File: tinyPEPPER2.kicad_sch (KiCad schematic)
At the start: 15 parts, among them U1 AP131-30

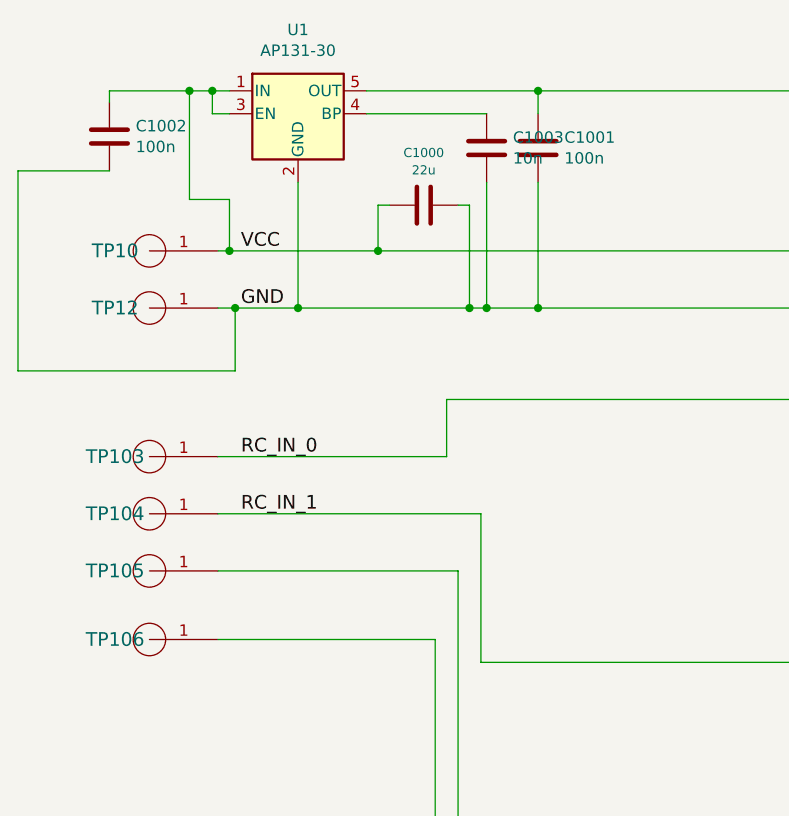
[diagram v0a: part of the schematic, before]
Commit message: cleaning up schematic
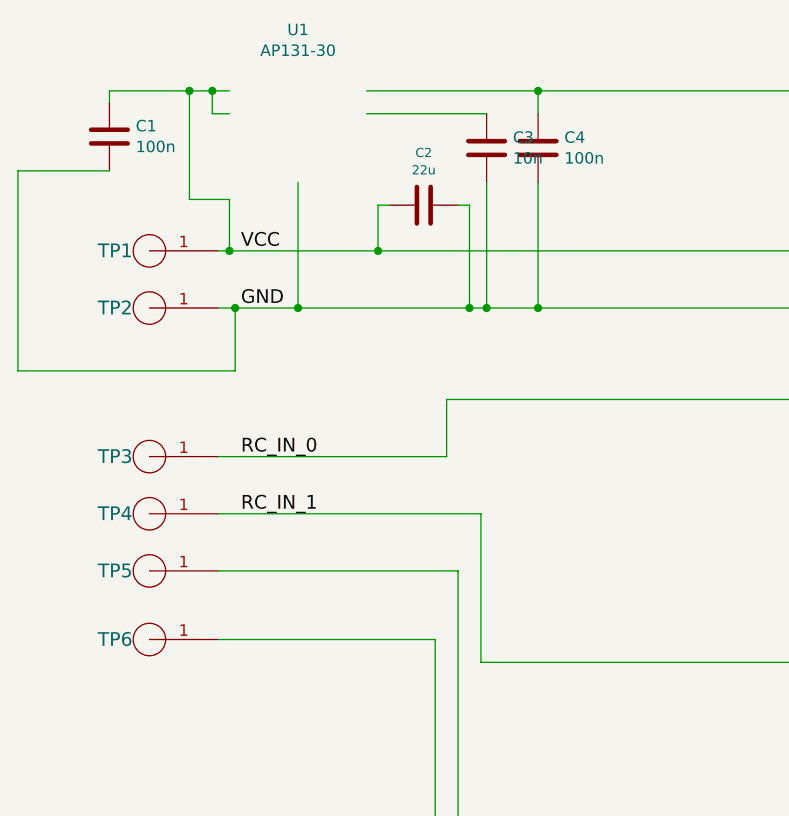
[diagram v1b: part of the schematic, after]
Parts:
- renumbered C1002 to C1, C1000 to C2, C1003 to C3, C1001 to C4, TP10 to TP1, TP12 to TP2, TP103 to TP3, TP104 to TP4, TP105 to TP5, TP106 to TP6
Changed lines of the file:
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@@
 		(in_pos_files yes)
 		(dnp no)
-		(property "Reference" "TP10"
+		(property "Reference" "TP1"
 			(at 36.83 62.23 0)
 			(show_name no)
@@
 			(project "tinyPEPPER2"
 				(path "/b5480a8a-eaf5-4e3b-b19a-0cc821568b0c"
-					(reference "TP10")
+					(reference "TP1")
 					(unit 1)
 				)
@@
 		(in_pos_files yes)
 		(dnp no)
-		(property "Reference" "TP12"
+		(property "Reference" "TP2"
 			(at 36.83 68.58 0)
 			(show_name no)
@@
 			(project "tinyPEPPER2"
 				(path "/b5480a8a-eaf5-4e3b-b19a-0cc821568b0c"
-					(reference "TP12")
+					(reference "TP2")
 					(unit 1)
 				)
@@
 		(in_pos_files yes)
 		(dnp no)
-		(property "Reference" "TP103"
+		(property "Reference" "TP3"
 			(at 36.83 85.09 0)
 			(show_name no)
@@
 			(project "tinyPEPPER2"
 				(path "/b5480a8a-eaf5-4e3b-b19a-0cc821568b0c"
-					(reference "TP103")
+					(reference "TP3")
 					(unit 1)
 				)
@@
 		(in_pos_files yes)
 		(dnp no)
-		(property "Reference" "TP104"
+		(property "Reference" "TP4"
 			(at 36.83 91.44 0)
 			(show_name no)
@@
 			(project "tinyPEPPER2"
 				(path "/b5480a8a-eaf5-4e3b-b19a-0cc821568b0c"
-					(reference "TP104")
+					(reference "TP4")
 					(unit 1)
 				)
@@
 		(in_pos_files yes)
 		(dnp no)
-		(property "Reference" "TP105"
+		(property "Reference" "TP5"
 			(at 36.83 97.79 0)
 			(show_name no)
@@
 			(project "tinyPEPPER2"
 				(path "/b5480a8a-eaf5-4e3b-b19a-0cc821568b0c"
-					(reference "TP105")
+					(reference "TP5")
 					(unit 1)
 				)
@@
 		(in_pos_files yes)
 		(dnp no)
-		(property "Reference" "TP106"
+		(property "Reference" "TP6"
 			(at 36.83 105.41 0)
 			(show_name no)
@@
 			(project "tinyPEPPER2"
 				(path "/b5480a8a-eaf5-4e3b-b19a-0cc821568b0c"
-					(reference "TP106")
+					(reference "TP6")
 					(unit 1)
 				)
@@
 		(in_pos_files yes)
 		(dnp no)
-		(property "Reference" "C1000"
+		(property "Reference" "C2"
 			(at 71.12 51.3334 90)
 			(show_name no)
@@
 			(project "tinyPEPPER2"
 				(path "/b5480a8a-eaf5-4e3b-b19a-0cc821568b0c"
-					(reference "C1000")
+					(reference "C2")
 					(unit 1)
 				)
@@
 		(in_pos_files yes)
 		(dnp no)
-		(property "Reference" "C1001"
+		(property "Reference" "C4"
 			(at 86.741 49.6316 0)
 			(show_name no)
@@
 			)
 		)
-		(instances
-			(project "tinyPEPPER2"
-				(path "/b5480a8a-eaf5-4e3b-b19a-0cc821568b0c"
-					(reference "C1001")
+		(pin "1"
+		)
+		(pin "2"
+		)
+		(instances
+			(project "tinyPEPPER2"
+				(path "/b5480a8a-eaf5-4e3b-b19a-0cc821568b0c"
+					(reference "C4")
 					(unit 1)
 				)
@@
 		(in_pos_files yes)
 		(dnp no)
-		(property "Reference" "C1002"
+		(property "Reference" "C1"
 			(at 39.116 48.3616 0)
 			(show_name no)
@@
 			)
 		)
-		(instances
-			(project "tinyPEPPER2"
-				(path "/b5480a8a-eaf5-4e3b-b19a-0cc821568b0c"
-					(reference "C1002")
+		(pin "1"
+		)
+		(pin "2"
+		)
+		(instances
+			(project "tinyPEPPER2"
+				(path "/b5480a8a-eaf5-4e3b-b19a-0cc821568b0c"
+					(reference "C1")
 					(unit 1)
 				)
@@
 		(in_pos_files yes)
 		(dnp no)
-		(property "Reference" "C1003"
+		(property "Reference" "C3"
 			(at 81.026 49.6316 0)
 			(show_name no)
@@
 			)
 		)
-		(instances
-			(project "tinyPEPPER2"
-				(path "/b5480a8a-eaf5-4e3b-b19a-0cc821568b0c"
-					(reference "C1003")
-					(unit 1)
-				)
+		(pin "1"
+		)
+		(pin "2"
+		)
+		(instances
+			(project "tinyPEPPER2"
+				(path "/b5480a8a-eaf5-4e3b-b19a-0cc821568b0c"
+					(reference "C3")
+					(unit 1)
+				)

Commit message: fix ap131-30
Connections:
- net GND: now also U1.2 (GND)
- net VCC: now also U1.1 (IN), U1.3 (EN)
- net single esc 1/3V3: now also U1.5 (OUT)
- net at C3.1: now also U1.4 (BP)

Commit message: add pwr lines to schematic
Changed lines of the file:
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@@
 	(paper "A4")
 	(title_block
-		(date "7 oct 2016")
+		(date "2026-10-02")
 	)
 	(junction
@@
 	)
 	(junction
+		(at 48.26 68.58)
+		(diameter 0)
+		(color 0 0 0 0)
+	)
+	(junction
 		(at 47.625 44.45)
 		(diameter 0)
@@
 	)
 	(junction
+		(at 48.26 62.23)
+		(diameter 0)
+		(color 0 0 0 0)
+	)
+	(junction
 		(at 45.085 44.45)
 		(diameter 0)
@@
 	(wire
 		(pts
+			(xy 30.48 58.42) (xy 48.26 58.42)
+		)
+		(stroke
+			(width 0)
+			(type default)
+		)
+	)
+	(wire
+		(pts
 			(xy 167.64 151.765) (xy 189.865 151.765)
 		)
@@
 	(wire
 		(pts
+			(xy 48.26 73.66) (xy 48.26 68.58)
+		)
+		(stroke
+			(width 0)
+			(type default)
+		)
+	)
+	(wire
+		(pts
 			(xy 48.26 68.58) (xy 119.38 68.58)
 		)
@@
 	(wire
 		(pts
+			(xy 48.26 58.42) (xy 48.26 62.23)
+		)
+		(stroke
+			(width 0)
+			(type default)
+		)
+	)
+	(wire
+		(pts
 			(xy 83.82 54.61) (xy 83.82 68.58)
 		)
@@
 		(pts
 			(xy 189.865 151.765) (xy 189.865 44.45)
+		)
+		(stroke
+			(width 0)
+			(type default)
+		)
+	)
+	(wire
+		(pts
+			(xy 29.21 73.66) (xy 48.26 73.66)
 		)
 		(stroke
@@
 			)
 		)
+		(pin "1"
+		)
+		(pin "2"
+		)
+		(pin "3"
+		)
+		(pin "4"
+		)
+		(pin "5"
+		)
 		(instances
 			(project "tinyPEPPER2"
@@
 					(unit 1)
 				)
+			)
+		)
+	)
+	(symbol
+		(lib_id "custom:PWR_FLAG")
+		(at 30.48 58.42 0)
+		(unit 1)
+		(body_style 1)
+		(exclude_from_sim no)
+		(in_bom yes)
+		(on_board yes)
+		(in_pos_files yes)
+		(dnp no)
+		(fields_autoplaced yes)
+		(property "Reference" "#FLG01"
+			(at 30.48 56.515 0)
+			(hide yes)
+			(show_name no)
+			(do_not_autoplace no)
+			(effects
+				(font
+					(size 1.27 1.27)
+				)
+			)
+		)
+		(property "Value" "PWR_FLAG"
+			(at 30.48 53.34 0)
+			(show_name no)
+			(do_not_autoplace no)
+			(effects
+				(font
+					(size 1.27 1.27)
+				)
+			)
+		)
+		(property "Footprint" ""
+			(at 30.48 58.42 0)
+			(hide yes)
+			(show_name no)
+			(do_not_autoplace no)
+			(effects
+				(font
+					(size 1.27 1.27)
+				)
+			)
+		)
+		(property "Datasheet" ""
+			(at 30.48 58.42 0)
+			(hide yes)
+			(show_name no)
+			(do_not_autoplace no)
+			(effects
+				(font
+					(size 1.27 1.27)
+				)
+			)
+		)
+		(property "Description" "Special symbol for telling ERC where power comes from"
+			(at 30.48 58.42 0)
+			(hide yes)
+			(show_name no)
+			(do_not_autoplace no)
+			(effects
+				(font
+					(size 1.27 1.27)
+				)
+			)
+		)
+		(pin "1"
+		)
+		(instances
+			(project "tinyPEPPER2"
+				(path "/b5480a8a-eaf5-4e3b-b19a-0cc821568b0c"
+					(reference "#FLG01")
+					(unit 1)
+				)
+			)
+		)
+	)
+	(symbol
+		(lib_id "custom:PWR_FLAG")
+		(at 29.21 73.66 0)
+		(unit 1)
+		(body_style 1)
+		(exclude_from_sim no)
+		(in_bom yes)
+		(on_board yes)
+		(in_pos_files yes)
+		(dnp no)
+		(fields_autoplaced yes)
+		(property "Reference" "#FLG02"
+			(at 29.21 71.755 0)
+			(hide yes)
+			(show_name no)
+			(do_not_autoplace no)
+			(effects
+				(font
+					(size 1.27 1.27)
+				)
+			)
+		)
+		(property "Value" "PWR_FLAG"
+			(at 29.21 68.58 0)
+			(show_name no)
+			(do_not_autoplace no)
+			(effects
+				(font
+					(size 1.27 1.27)
+				)
+			)
+		)
+		(property "Footprint" ""
+			(at 29.21 73.66 0)
+			(hide yes)
+			(show_name no)
+			(do_not_autoplace no)
+			(effects
+				(font
+					(size 1.27 1.27)
+				)
+			)
+		)
+		(property "Datasheet" ""
+			(at 29.21 73.66 0)
+			(hide yes)
+			(show_name no)
+			(do_not_autoplace no)
+			(effects
+				(font
+					(size 1.27 1.27)
+				)
+			)
+		)
+		(property "Description" "Special symbol for telling ERC where power comes from"
+			(at 29.21 73.66 0)
+			(hide yes)
+			(show_name no)
+			(do_not_autoplace no)
+			(effects
+				(font
+					(size 1.27 1.27)
+				)
+			)
+		)
+		(pin "1"
+		)
+		(instances
+			(project "tinyPEPPER2"
+				(path "/b5480a8a-eaf5-4e3b-b19a-0cc821568b0c"
+					(reference "#FLG02")
+					(unit 1)
+				)
